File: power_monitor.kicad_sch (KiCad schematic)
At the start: 20 parts, among them U12 ATtiny25-20SS

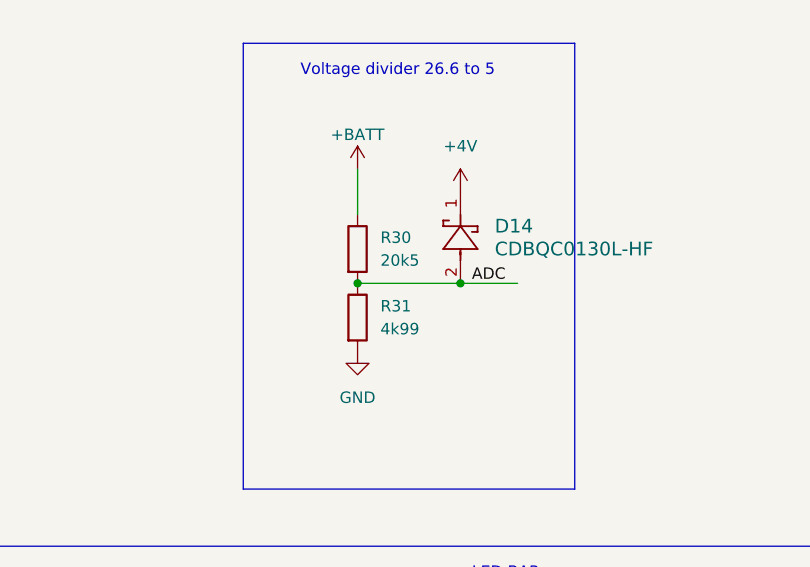
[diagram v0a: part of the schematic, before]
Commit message: change flash to sd flash, cleanup, and reconcile with F405FC
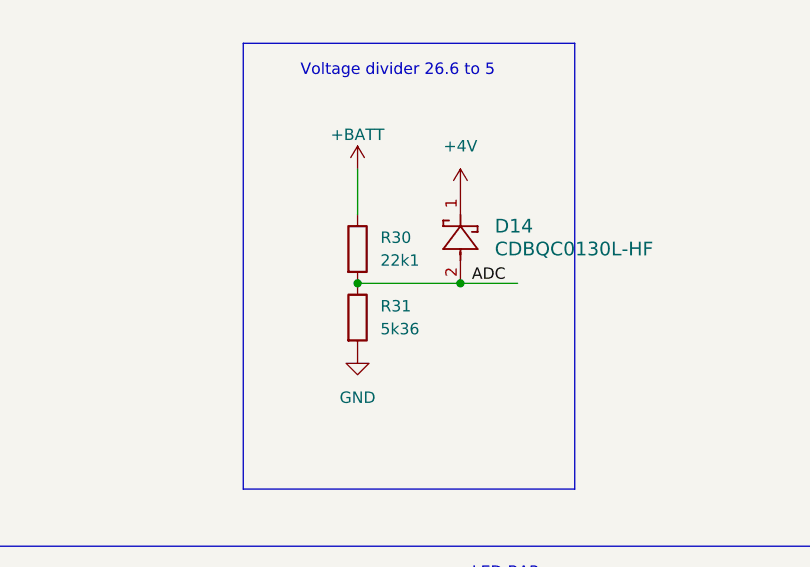
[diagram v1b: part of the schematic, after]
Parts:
- R30: value 20k5 -> 22k1
- R31: value 4k99 -> 5k36
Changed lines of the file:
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@@
 		(fields_autoplaced yes)
 		(property "Reference" "R31"
-			(at 147.32 87.63 0)
+			(at 147.32 87.6299 0)
 			(effects
 				(font
@@
 			)
 		)
-		(property "Value" "4k99"
-			(at 147.32 90.17 0)
+		(property "Value" "5k36"
+			(at 147.32 90.1699 0)
 			(effects
 				(font
@@
 		(fields_autoplaced yes)
 		(property "Reference" "R30"
-			(at 147.32 80.01 0)
+			(at 147.32 80.0099 0)
 			(effects
 				(font
@@
 			)
 		)
-		(property "Value" "20k5"
-			(at 147.32 82.55 0)
-			(effects
-				(font
+		(property "Value" "22k1"
+			(at 147.32 82.5499 0)
+			(effects
+				(font
